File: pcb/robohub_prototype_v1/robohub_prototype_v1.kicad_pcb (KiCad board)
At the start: 10 copper layers, 102 parts, among them J21 Barrel_Jack_Switch_Pin3Ring, J51 USB_A, J52 USB_A, J71 USB_A, U1 ATSAMA5D27C, U21 LM3880, U22 TPS564242DRL, U23 TPS564242DRL, U24 TPS564242DRL, U25 TPS564242DRL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

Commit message: Updates to DDR2 routing on inner layers
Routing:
- net /DDR2_3/DDR_A13: track 10.6 -> 56.0 mm, vias 2 -> 3
- net /DDR2_3/DDR_A7: track 13.7 -> 57.5 mm, vias 2 -> 3
- net /DDR2_3/DDR_WE: track 9.95 -> 45.2 mm, vias 2 -> 3
- net /DDR2_3/DDR_BA0: track 15.3 -> 46.7 mm, vias 2 -> 3
- net /DDR2_3/DDR_A6: track 10.7 -> 41.9 mm, vias 2 -> 3
- net /DDR2_3/DDR_A9: track 8.54 -> 39.3 mm, vias 2 -> 3
- net /DDR2_3/DDR_A5: track 14.5 -> 44.5 mm, vias 2 -> 3
- net /DDR2_3/DDR_BA1: track 13.8 -> 43.2 mm, vias 2 -> 3
- net /DDR2_3/DDR_A0: track 10.0 -> 35.4 mm, vias 2 -> 3
- net /DDR2_3/DDR_CAS: track 9.98 -> 33.7 mm, vias 2 -> 3
- net /DDR2_3/DDR_CS: track 11.6 -> 33.2 mm, vias 2 -> 3
- net /DDR2_3/DDR_RAS: track 9.58 -> 29.3 mm, vias 2 -> 3
- net /DDR2_3/DDR_A8: track 47.0 -> 50.4 mm

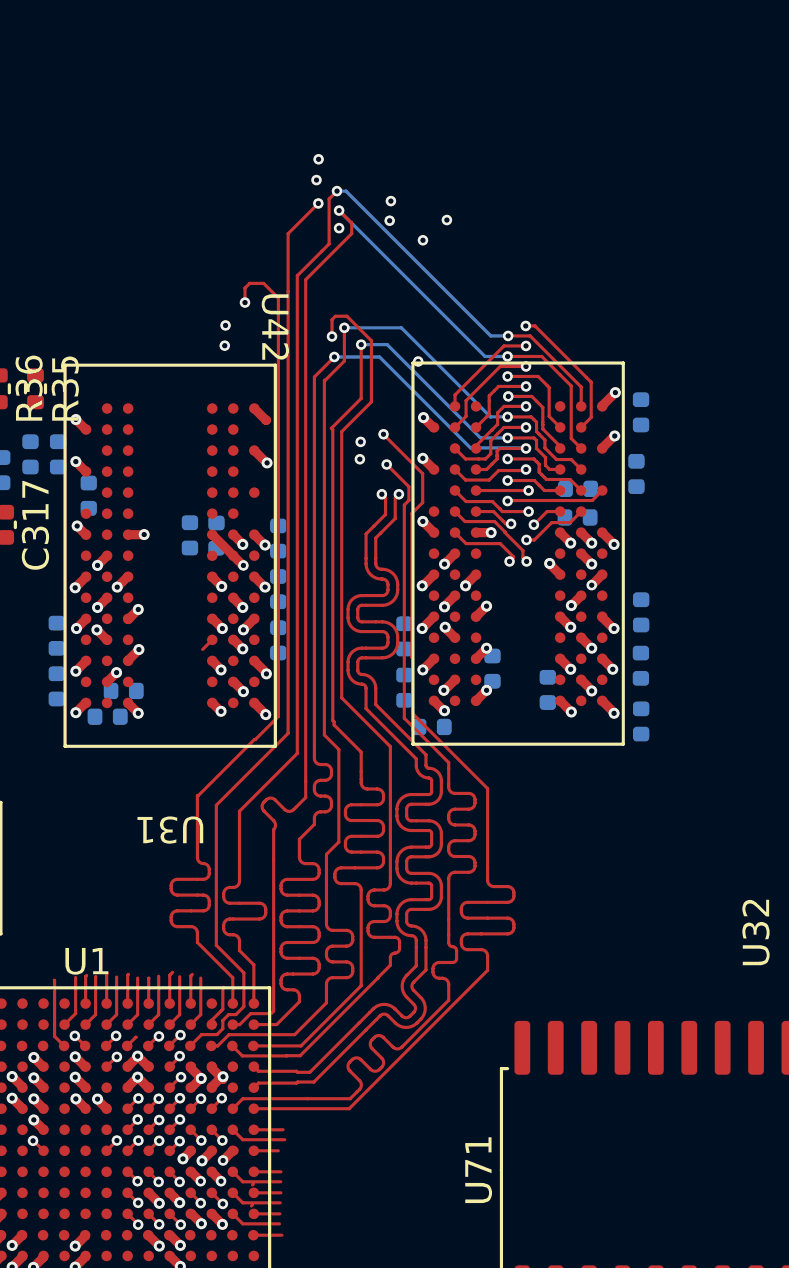
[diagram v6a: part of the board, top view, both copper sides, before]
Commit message: Addd updated DDR2 routingg
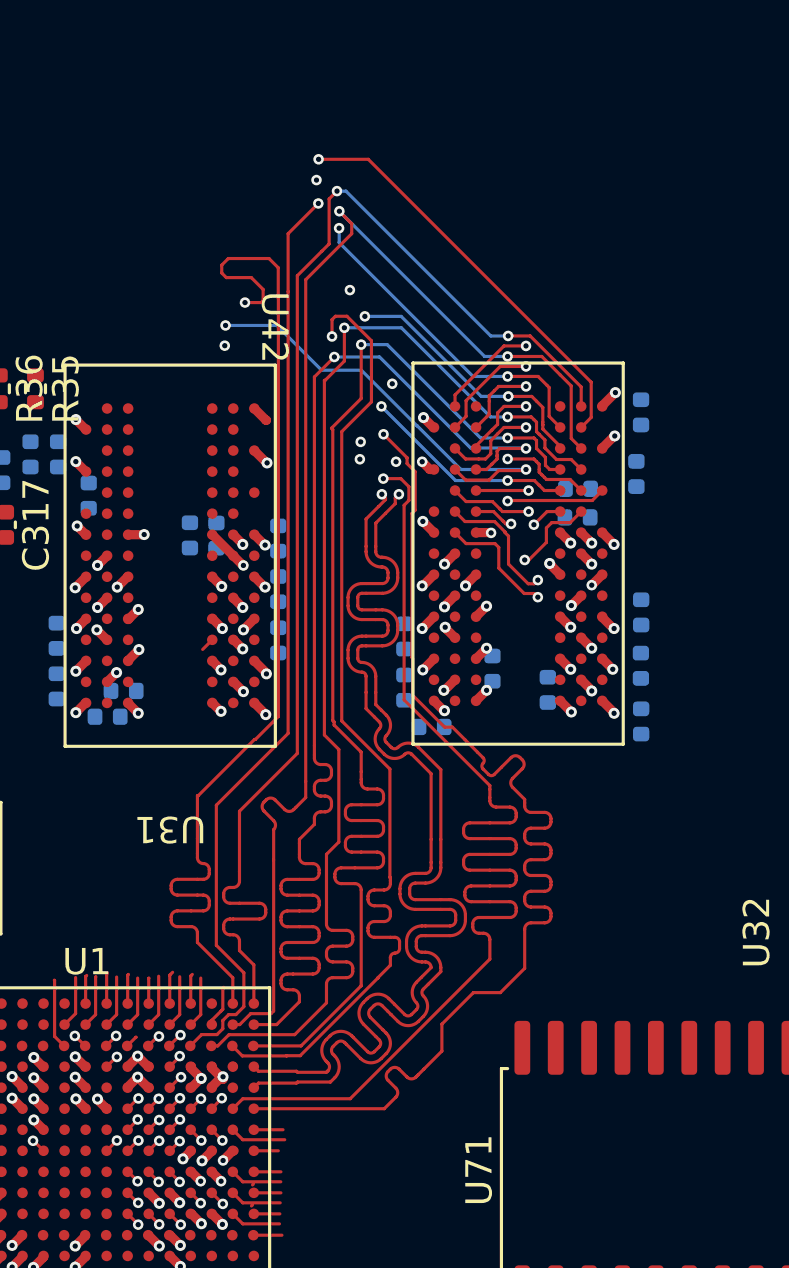
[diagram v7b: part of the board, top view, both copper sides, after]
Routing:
- net /DDR2_3/DDR_CAS: track 33.7 -> 47.6 mm
- net /DDR2_3/DDR_A0: track 35.4 -> 49.1 mm
- net /DDR2_3/DDR_A9: track 39.3 -> 48.3 mm
- net /DDR2_3/DDR_CS: track 33.2 -> 41.6 mm
- net /DDR2_3/DDR_RAS: track 29.3 -> 37.2 mm
- net /DDR2_3/DDR_CLK+: track 47.8 -> 55.2 mm
- net /DDR2_3/DDR_CKE: track 49.5 -> 56.4 mm
- net /DDR2_3/DDR_BA2: track 49.9 -> 56.5 mm
- net /DDR2_3/DDR_A5: track 44.5 -> 51.1 mm
- net /DDR2_3/DDR_CLK-: track 49.6 -> 55.8 mm
- net /DDR2_3/DDR_BA1: track 43.2 -> 49.3 mm
- net /DDR2_3/DDR_A11: track 50.5 -> 55.9 mm
- net /DDR2_3/DDR_A6: track 41.9 -> 45.9 mm
- net /DDR2_3/DDR_WE: track 45.2 -> 43.1 mm
- net /DDR2_3/DDR_BA0: track 46.7 -> 48.1 mm
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
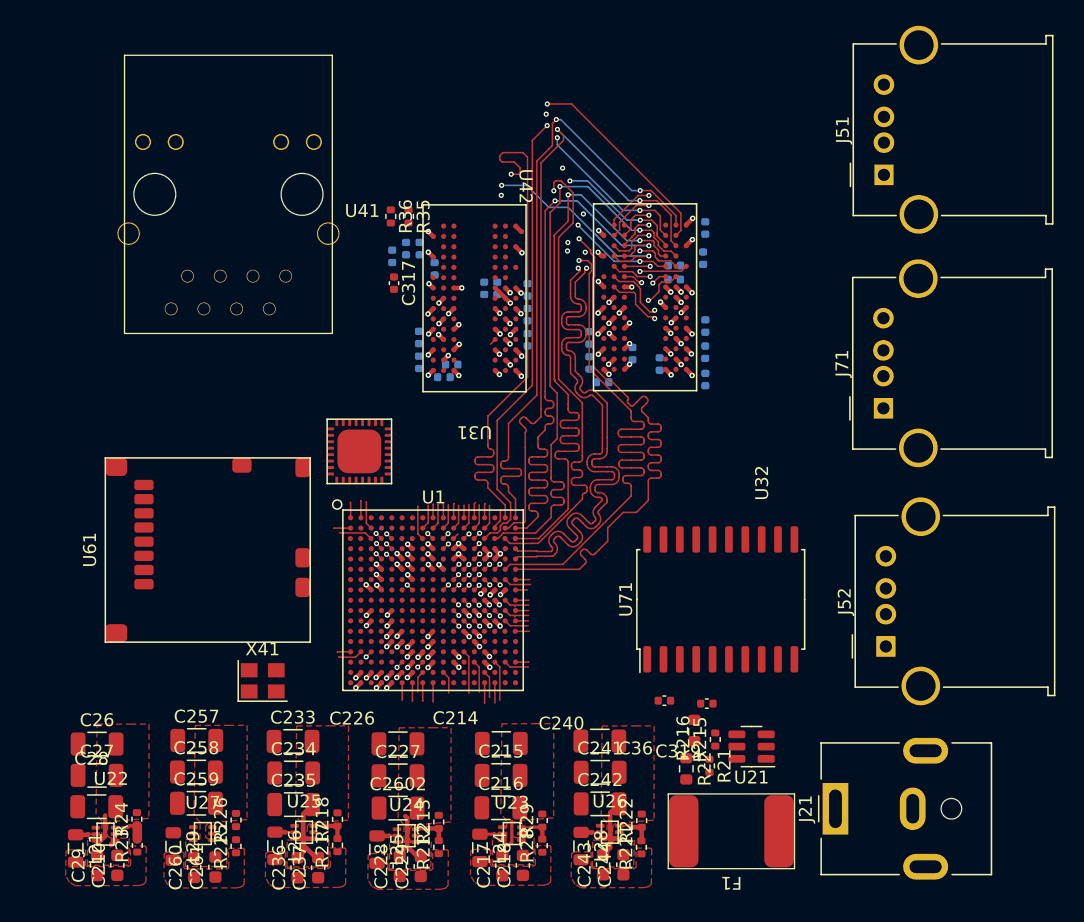
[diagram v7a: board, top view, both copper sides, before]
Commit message: Add updated PCB routing for data byte lanes
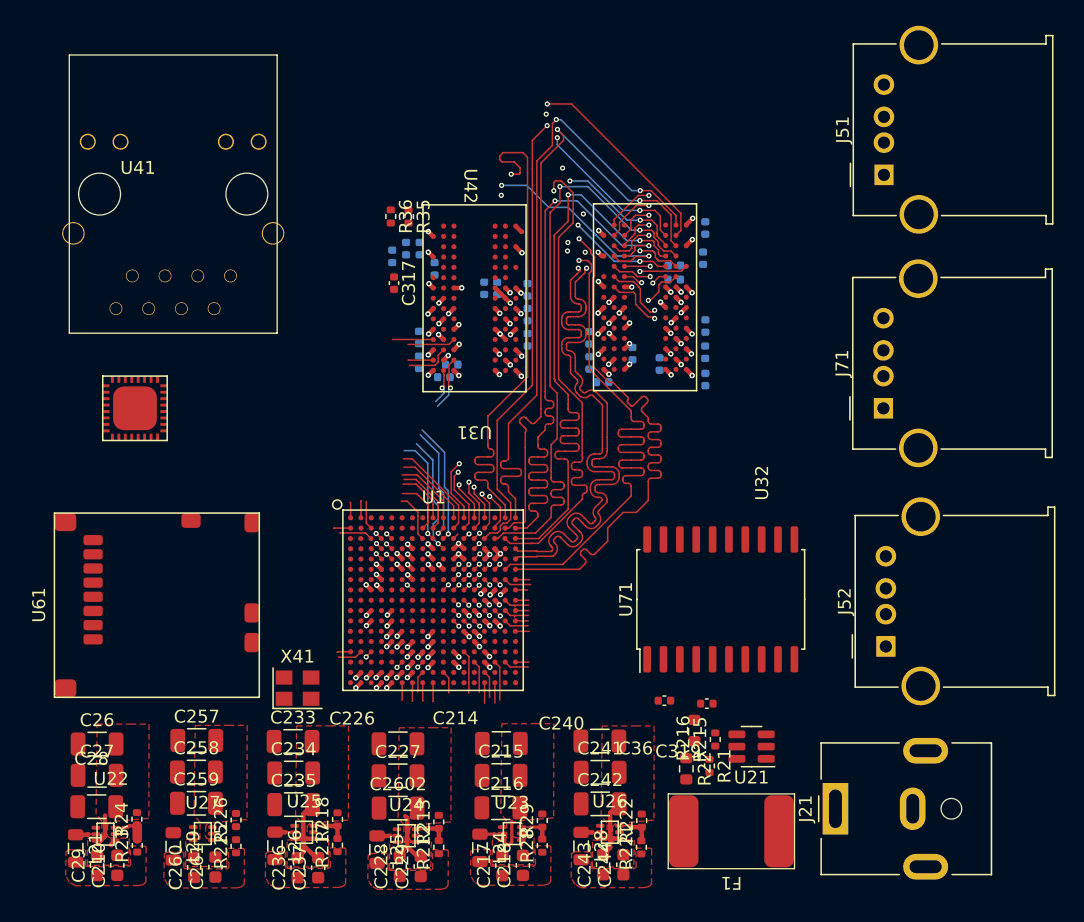
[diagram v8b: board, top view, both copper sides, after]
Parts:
- moved U41 17.7 mm to (98.7, 79.8)
- moved U61 5.82 mm to (100.4, 95.1)
- moved U42 4.29 mm to (101.7, 63.2)
- moved X41 2.76 mm to (111.3, 101.5)
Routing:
- net /DDR2_3/DDR_DQS2+: track 0.61 -> 13.7 mm, vias 1 -> 2
- net /DDR2_3/DDR_D21: track 0.60 -> 12.5 mm
- net /DDR2_3/DDR_D18: track 0.62 -> 12.0 mm
- net /DDR2_3/DDR_DQS2-: track 1.97 -> 12.0 mm, vias 0 -> 2
- net /DDR2_3/DDR_D23: track 1.12 -> 8.00 mm
- net /DDR2_3/DDR_D16: track 1.96 -> 7.78 mm
- net /DDR2_3/DDR_D22: track 1.93 -> 7.73 mm
- net /DDR2_3/DDR_D20: track 1.17 -> 5.34 mm
- net /DDR2_3/DDR_D1: track 0.97 -> 4.87 mm, vias 0 -> 1
- net /DDR2_3/DDR_D17: track 1.98 -> 5.58 mm
- net /DDR2_3/DDR_D0: track 2.00 -> 5.09 mm, vias 0 -> 1
- net /DDR2_3/DDR_D19: track 1.60 -> 4.18 mm
- net /DDR2_3/DDR_DQS0+: track 1.98 -> 4.05 mm, vias 0 -> 1
- net /DDR2_3/DDR_D3: track 1.24 -> 3.04 mm, vias 0 -> 1
- net /DDR2_3/DDR_D4: track 1.13 -> 2.72 mm, vias 0 -> 1
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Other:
- board text added: "${REFERENCE}"
